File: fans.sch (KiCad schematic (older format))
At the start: 17 parts, among them M1 300, M2 300, M3 300, Q1 BC549, Q2 BC549, Q3 BC549, U1 Adafruit_Huzzah, U2 LD1117AV33

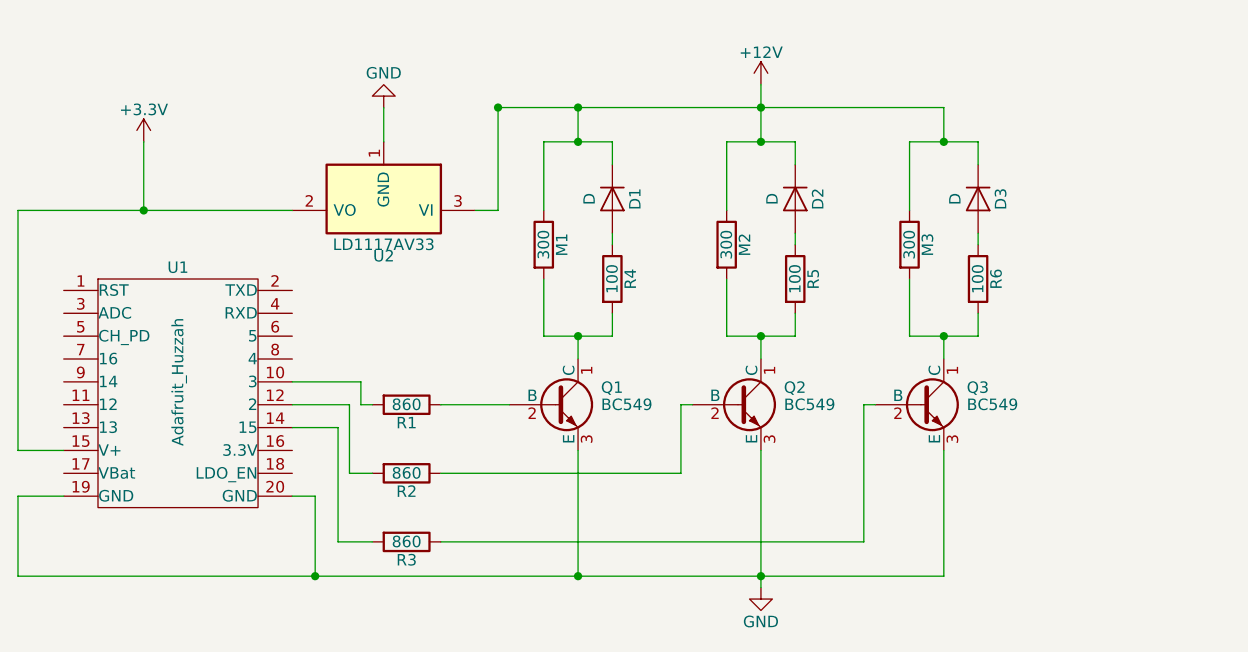
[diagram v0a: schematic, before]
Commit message: Add footprint and layout
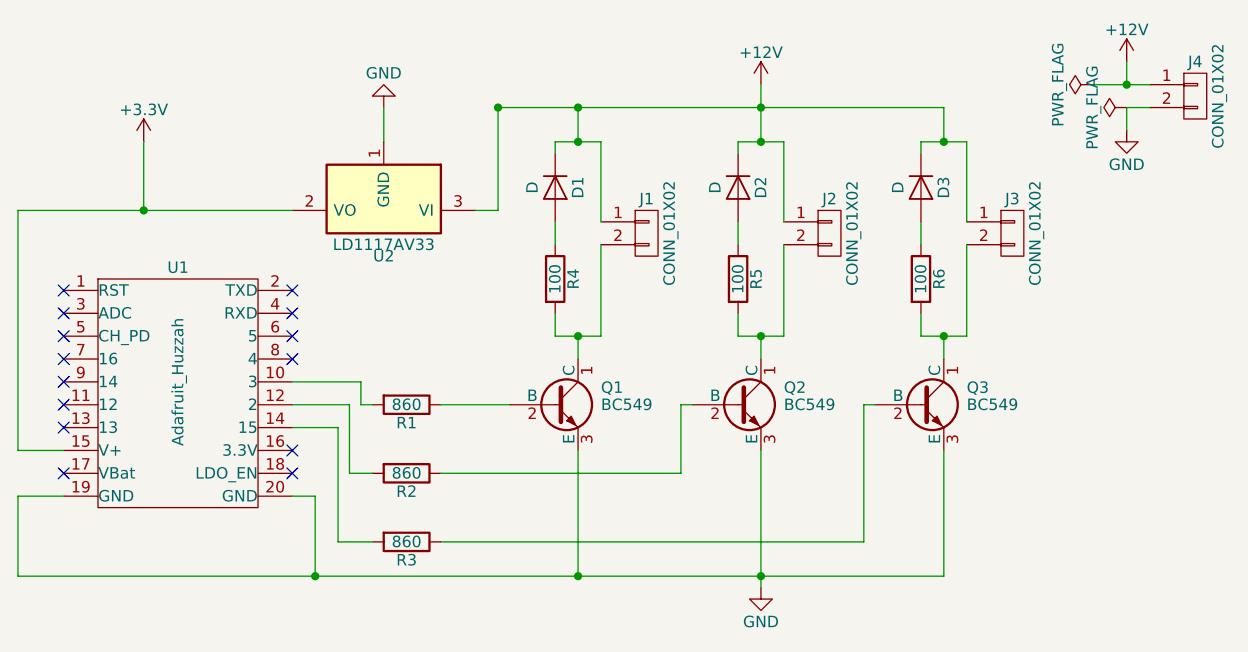
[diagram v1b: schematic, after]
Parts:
- removed D2: D, Diodes_THT:D_DO-27_P12.70mm_Horizontal, symbol D
- removed M1, M2, M3: 300, Pin_Headers:Pin_Header_Straight_1x02, symbol R
- removed R5: 100, Resistors_THT:R_Axial_DIN0414_L11.9mm_D4.5mm_P15.24mm_Horizontal, symbol R
- added D1: D, Diodes_ThroughHole:D_A-405_P7.62mm_Horizontal, symbol D
- added J1, J2, J3, J4: CONN_01X02, Pin_Headers:Pin_Header_Straight_1x02_Pitch2.54mm, symbol CONN_01X02
- added R4: 100, Resistors_ThroughHole:R_Axial_DIN0207_L6.3mm_D2.5mm_P10.16mm_Horizontal, symbol R
- D2: renamed from D1; footprint Diodes_THT:D_DO-27_P12.70mm_Horizontal -> Diodes_ThroughHole:D_A-405_P7.62mm_Horizontal
- D3: footprint Diodes_THT:D_DO-27_P12.70mm_Horizontal -> Diodes_ThroughHole:D_A-405_P7.62mm_Horizontal
- R1, R2, R3, R6: footprint Resistors_THT:R_Axial_DIN0414_L11.9mm_D4.5mm_P15.24mm_Horizontal -> Resistors_ThroughHole:R_Axial_DIN0207_L6.3mm_D2.5mm_P10.16mm_Horizontal
- R5: renamed from R4; footprint Resistors_THT:R_Axial_DIN0414_L11.9mm_D4.5mm_P15.24mm_Horizontal -> Resistors_ThroughHole:R_Axial_DIN0207_L6.3mm_D2.5mm_P10.16mm_Horizontal
- U1: footprint Pin_Headers:Pin_Header_Angled_2x10_Pitch2.54mm -> Adafruit_Huzzah:Adafruit_Huzzah_ESP8266_Breakout
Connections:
- net +12V: now also D1.1 (K), J1.1 (P1), J2.1 (P1), J3.1 (P1), J4.1 (P1)
- net GND: now also J4.2 (P2)
- net at Q1.1 (C): now also J1.2 (P2), R4.2; no longer R5.2
- net at Q3.1 (C), R6.2: now also J3.2 (P2)
- net at Q2.1 (C): now also R5.2, J2.2 (P2)
- new net: D1.2 (A), R4.1
- no-connect marks 0 -> 14
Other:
- moved on the sheet: D2, R5

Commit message: Wider traces.
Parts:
- Q1, Q2, Q3: footprint TO_SOT_Packages_THT:TO-92_Molded_Narrow -> TO_SOT_Packages_THT:TO-92_Molded_Wide_Oval
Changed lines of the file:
@@
 F 0 "Q1" H 5850 2925 50  0000 L CNN
 F 1 "BC549" H 5850 2850 50  0000 L CNN
-F 2 "TO_SOT_Packages_THT:TO-92_Molded_Narrow" H 5850 2775 50  0001 L CIN
+F 2 "TO_SOT_Packages_THT:TO-92_Molded_Wide_Oval" H 5850 2775 50  0001 L CIN
 F 3 "" H 5650 2850 50  0001 L CNN
 	1    5650 2850
@@
 F 0 "Q3" H 7450 2925 50  0000 L CNN
 F 1 "BC549" H 7450 2850 50  0000 L CNN
-F 2 "TO_SOT_Packages_THT:TO-92_Molded_Narrow" H 7450 2775 50  0001 L CIN
+F 2 "TO_SOT_Packages_THT:TO-92_Molded_Wide_Oval" H 7450 2775 50  0001 L CIN
 F 3 "" H 7250 2850 50  0001 L CNN
 	1    7250 2850
@@
 F 0 "Q2" H 6650 2925 50  0000 L CNN
 F 1 "BC549" H 6650 2850 50  0000 L CNN
-F 2 "TO_SOT_Packages_THT:TO-92_Molded_Narrow" H 6650 2775 50  0001 L CIN
+F 2 "TO_SOT_Packages_THT:TO-92_Molded_Wide_Oval" H 6650 2775 50  0001 L CIN
 F 3 "" H 6450 2850 50  0001 L CNN
 	1    6450 2850
